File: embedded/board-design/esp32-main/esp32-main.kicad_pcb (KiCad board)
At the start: 2 copper layers, 84 parts, among them J1 Conn_ARM_JTAG_SWD_10, J2 Conn_01x08_Socket, J3 Conn_01x08_Socket, J4 0473460001, J5 Conn_01x03_Socket, Q1 BC817, Q2 BC817, Q3 FDN340P, Q4 FMMT720TA, Q5 FDN340P, Q6 FDN340P, U1 ESP32-WROVER-E, U2 BD48ExxG, U3 FT231XS, U4 TPS61090, U5 LTC4054ES5-4.2

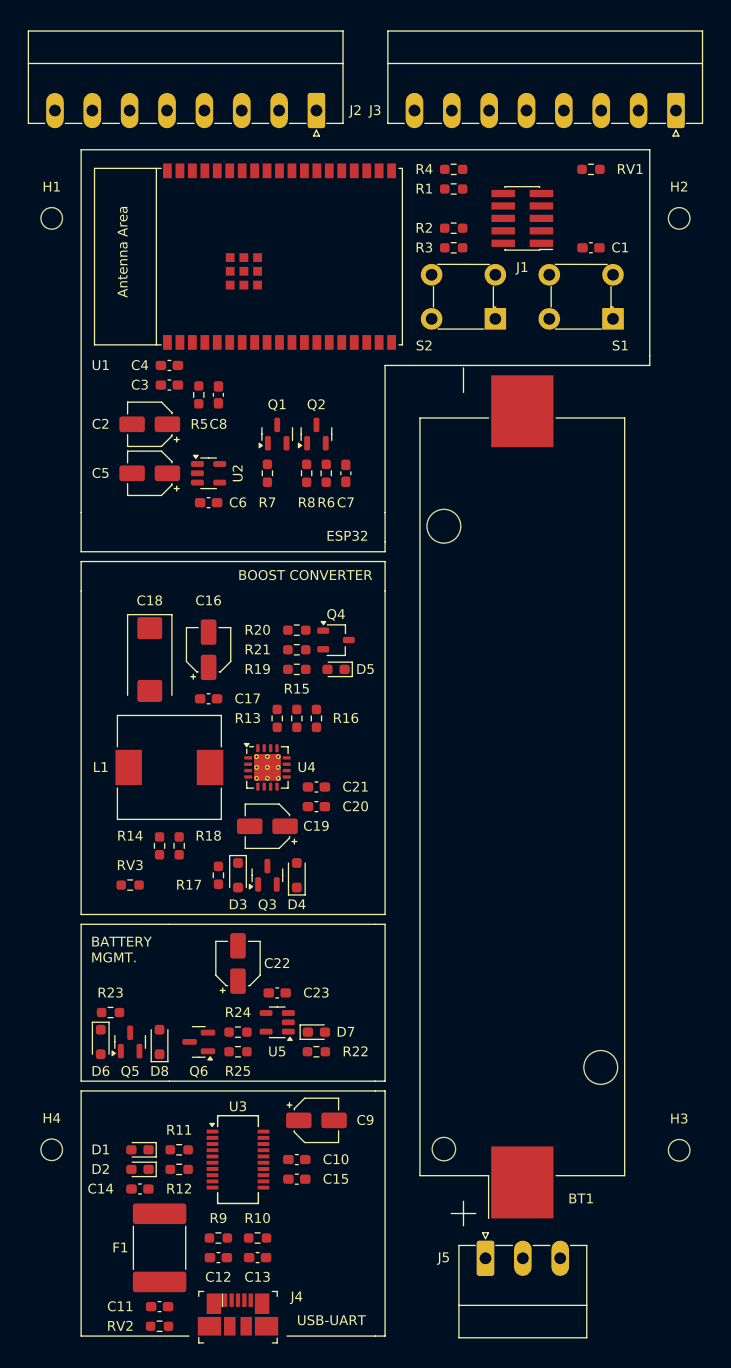
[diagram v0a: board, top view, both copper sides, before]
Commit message: [bike-embedded-app]
Finished first draft of the embedded hardware app. PCB design
constraints follow PCBWay recommendations.

Signed-off-by: Nicolae-Andrei Vasile <vasilenicolaeandrei@gmail.com>
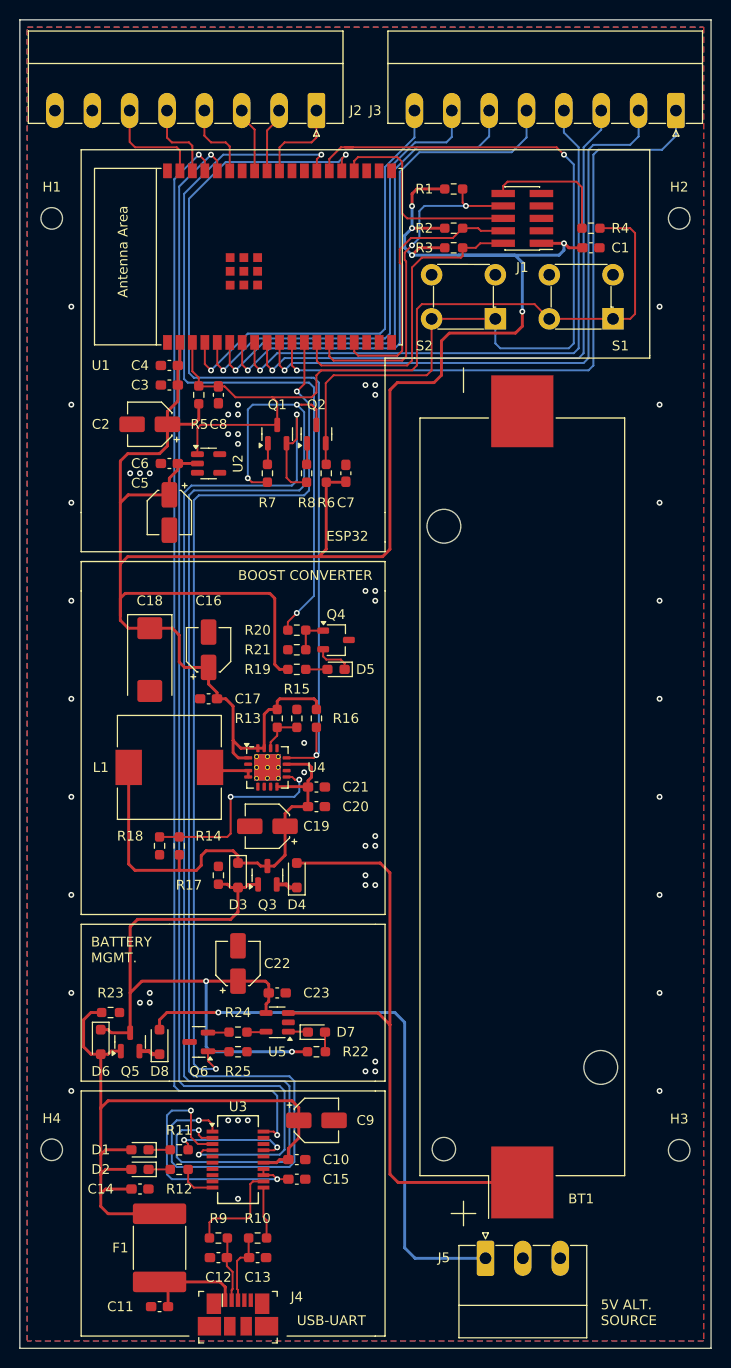
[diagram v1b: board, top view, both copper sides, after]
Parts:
- removed RV1, RV2, RV3: V5.5MLA0603N, Resistor_SMD:R_0603_1608Metric_Pad0.98x0.95mm_HandSolder
- moved R4 15.2 mm to (168.0, 42.0), turned to 0 degrees
- moved C6 5.66 mm to (125.0, 66.0), turned to 180 degrees
- moved C5 4.47 mm to (125.0, 71.0), turned to -90 degrees
- moved R14 2.00 mm to (126.0, 105.0)
- moved R18 2.00 mm to (124.0, 105.0)
- moved U2 1.00 mm to (129.0, 66.0)
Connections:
- J2 pad 1: /GPIO32 -> /GPIO5/VSPICS0
- J2 pad 2: /GPIO33 -> /GPIO18/VSPICLK
- J2 pad 3: unconnected-(J2-Pin_3-Pad3) -> /GPIO19/VSPIQ
- J2 pad 4: unconnected-(J2-Pin_4-Pad4) -> /GPIO21/VSPIHD
- J2 pad 5: /GPIO34 -> /GPIO22/VSPIWP
- J2 pad 6: /GPIO35 -> /GPIO23/VSPID
- J2 pad 7: /GPIO36 -> unconnected-(J2-Pin_7-Pad7)
- J2 pad 8: /GPIO39 -> unconnected-(J2-Pin_8-Pad8)
- J3 pad 3: /GPIO23/VSPID -> /GPIO33
- J3 pad 4: /GPIO22/VSPIWP -> /GPIO32
- J3 pad 5: /GPIO21/VSPIHD -> /GPIO35
- J3 pad 6: /GPIO19/VSPIQ -> /GPIO34
- J3 pad 7: /GPIO18/VSPICLK -> /GPIO39
- J3 pad 8: /GPIO5/VSPICS0 -> /GPIO36
- J4 pad SH: Earth_Protective -> GND
- J5 pad 3: Earth_Protective -> GND
- U4 pad 17: Earth_Protective -> GND
- U4 pad 5: Earth_Protective -> GND
- U4 pad 6: Earth_Protective -> GND
- U4 pad 7: Earth_Protective -> GND
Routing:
- net +3V3: track 0.00 -> 237.9 mm, vias 0 -> 5
- net /usb-uart/~{DTR}: track 0.00 -> 139.0 mm, vias 0 -> 3
- net /U0RXD: track 0.00 -> 125.5 mm, vias 0 -> 2
- net /usb-uart/~{RTS}: track 0.00 -> 124.8 mm, vias 0 -> 2
- net /U0TXD: track 0.00 -> 114.4 mm, vias 0 -> 2
- net /power-supply/LDO: track 0.00 -> 95.7 mm, vias 0 -> 2
- net /battery/~{SHDN}: track 0.00 -> 92.4 mm, vias 0 -> 2
- net /BOOT: track 0.00 -> 89.6 mm, vias 0 -> 1
- net Net-(Q1-C): track 0.00 -> 84.8 mm
- net /power-supply/PWRLED: track 0.00 -> 75.8 mm, vias 0 -> 2
- net VBUS: track 0.00 -> 70.2 mm
- net +5V: track 0.00 -> 67.4 mm, vias 0 -> 2
- net /GPIO26: track 0.00 -> 66.8 mm, vias 0 -> 1
- net VBAT: track 0.00 -> 65.4 mm
- net /GPIO25: track 0.00 -> 64.1 mm, vias 0 -> 1
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- added copper zone on B.Cu, net GND
- added copper zone on F.Cu, net GND
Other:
- board outline added: 70.5 x 135.5 mm
- board text added: "5V ALT. SOURCE"
